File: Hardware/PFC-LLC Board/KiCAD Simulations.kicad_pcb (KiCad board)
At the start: 2 copper layers, 157 x 79.5 mm, 42 parts, among them J1 1792229, J2 Conn_01x02_Female, J3 1792229, Q1 C2M0160120D, U1 UCC28180DR

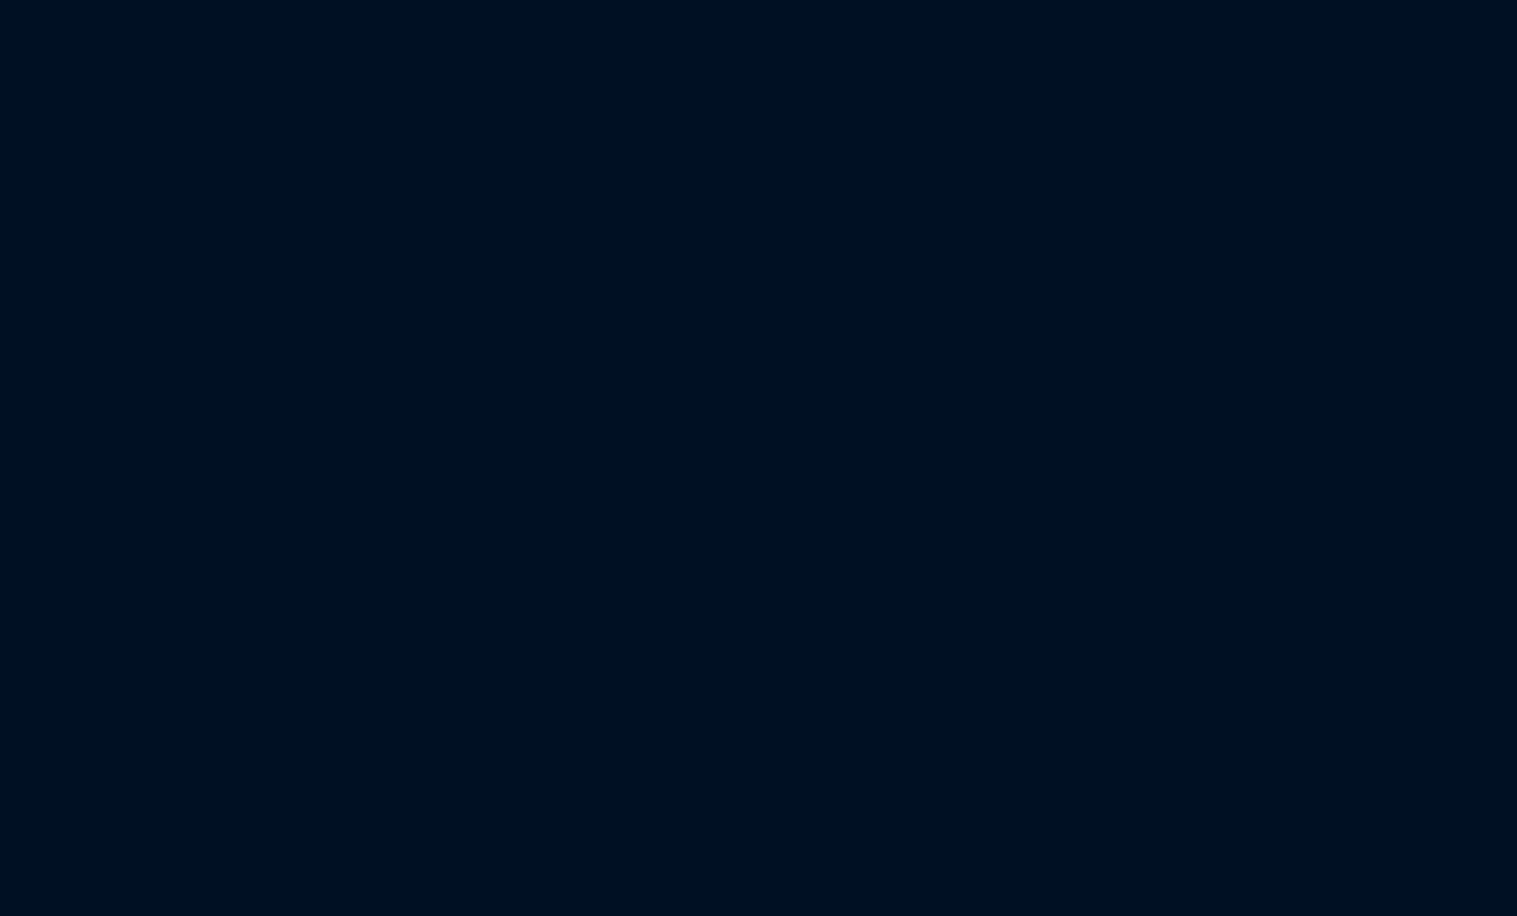
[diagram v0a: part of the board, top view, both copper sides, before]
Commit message: LLC PCB ready w/ PFC board
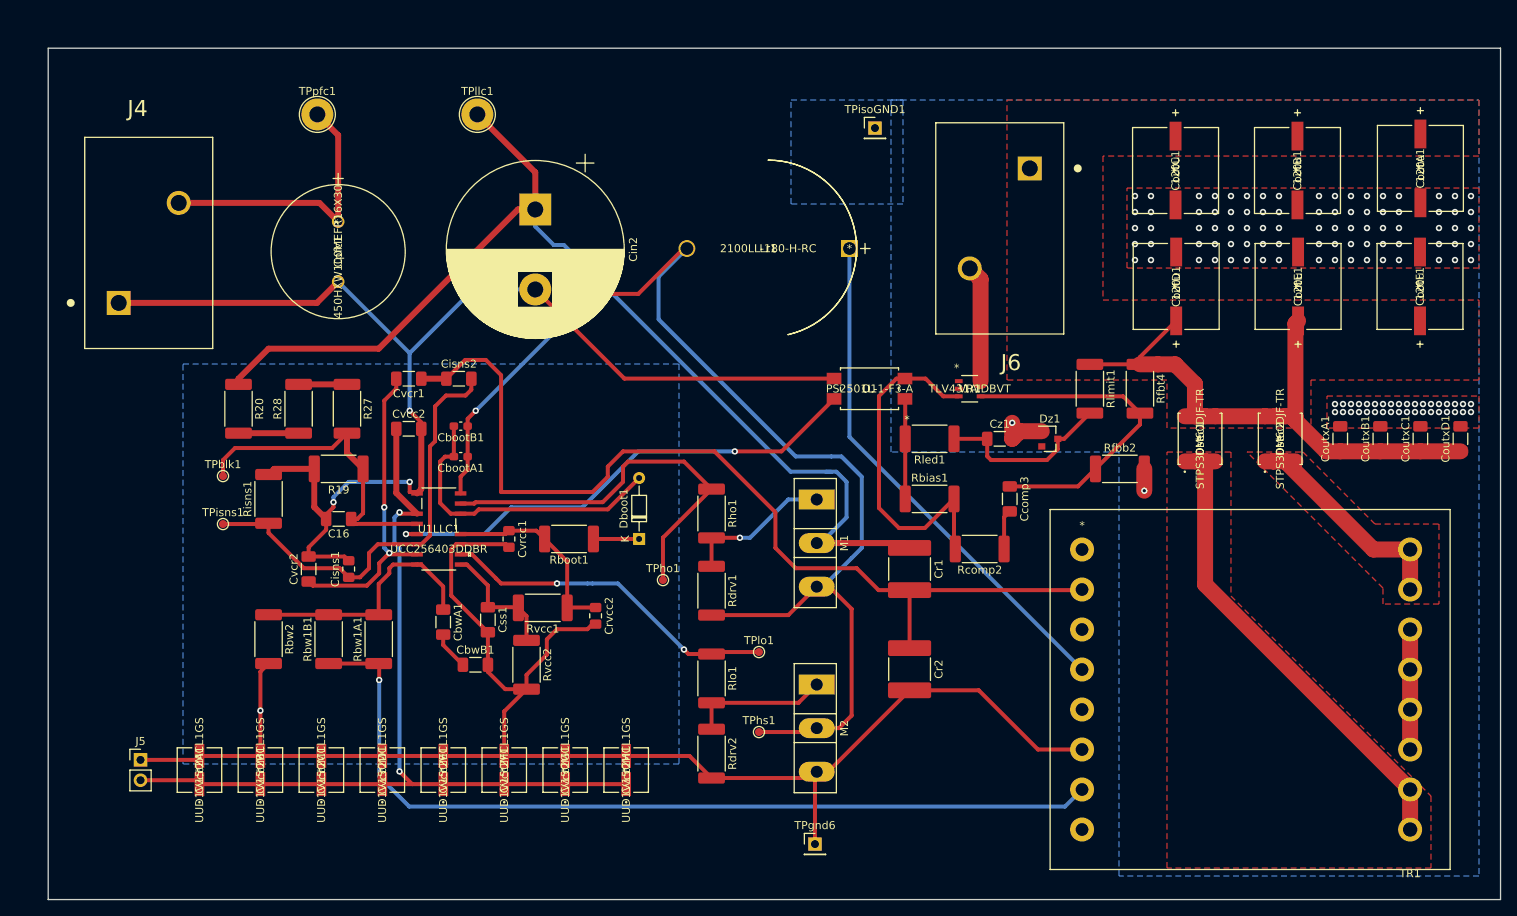
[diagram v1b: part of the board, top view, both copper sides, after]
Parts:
- added C16: 220p, Capacitor_SMD:C_1206_3216Metric_Pad1.33x1.80mm_HandSolder, F.Cu at (131.5, 384.4)
- added CbootA1: 470n, Capacitor_SMD:C_0603_1608Metric_Pad1.08x0.95mm_HandSolder, F.Cu at (146.7, 376.6)
- added CbootB1: 470n, Capacitor_SMD:C_0603_1608Metric_Pad1.08x0.95mm_HandSolder, F.Cu at (146.7, 372.8)
- added CbwA1: 12p, Capacitor_SMD:C_1206_3216Metric_Pad1.33x1.80mm_HandSolder, F.Cu at (144.5, 397.3)
- added CbwB1: 12p, Capacitor_SMD:C_1206_3216Metric_Pad1.33x1.80mm_HandSolder, F.Cu at (148.6, 402.6)
- added Ccomp3: 2.7n, Capacitor_SMD:C_1206_3216Metric_Pad1.33x1.80mm_HandSolder, F.Cu at (215.3, 381.9)
- added Cin2: 47u, Capacitor_THT:CP_Radial_D22.0mm_P10.00mm_SnapIn, F.Cu at (156.0, 345.7)
- added Cisns1: 3.3p, Capacitor_SMD:C_0805_2012Metric_Pad1.18x1.45mm_HandSolder, F.Cu at (132.7, 390.6)
- added Cisns2: 220p, Capacitor_SMD:C_1206_3216Metric_Pad1.33x1.80mm_HandSolder, F.Cu at (146.5, 366.8)
- added CoutA1: 120u, LLC_Cout:35SVPF120M, F.Cu at (266.7, 340.5)
- added CoutB1: 120u, LLC_Cout:35SVPF120M, F.Cu at (251.3, 340.8)
- added CoutC1: 120u, LLC_Cout:35SVPF120M, F.Cu at (236.1, 340.8)
- added CoutD1: 120u, LLC_Cout:35SVPF120M, F.Cu at (236.1, 355.3)
- added CoutE1: 120u, LLC_Cout:35SVPF120M, F.Cu at (251.4, 355.3)
- added CoutF1: 120u, LLC_Cout:35SVPF120M, F.Cu at (266.6, 355.3)
- added CoutxA1: 22u, Capacitor_SMD:C_1206_3216Metric_Pad1.33x1.80mm_HandSolder, F.Cu at (256.7, 374.3)
- added CoutxB1: 22u, Capacitor_SMD:C_1206_3216Metric_Pad1.33x1.80mm_HandSolder, F.Cu at (261.7, 374.3)
- added CoutxC1: 22u, Capacitor_SMD:C_1206_3216Metric_Pad1.33x1.80mm_HandSolder, F.Cu at (266.7, 374.3)
- added CoutxD1: 22u, Capacitor_SMD:C_1206_3216Metric_Pad1.33x1.80mm_HandSolder, F.Cu at (271.7, 374.3)
- added Cpfc1: 450HXW100MEFR16X30, LLC_pfc:450HXW100MEFR16X30, F.Cu at (131.4, 347.2)
- added Cr1: 150n, Capacitor_SMD:C_2220_5650Metric_Pad1.97x5.40mm_HandSolder, F.Cu at (202.8, 390.6)
- added Cr2: 150n, Capacitor_SMD:C_2220_5650Metric_Pad1.97x5.40mm_HandSolder, F.Cu at (202.8, 403.1)
- added Crvcc2: 4.7u, Capacitor_SMD:C_0805_2012Metric_Pad1.18x1.45mm_HandSolder, F.Cu at (163.6, 396.5)
- added Css1: 150n, Capacitor_SMD:C_1206_3216Metric_Pad1.33x1.80mm_HandSolder, F.Cu at (150.1, 397.0)
- added Cvcc2: 2.2u, Capacitor_SMD:C_1206_3216Metric_Pad1.33x1.80mm_HandSolder, F.Cu at (140.2, 373.1)
- added Cvcc2A1: UUD1V150MCL1GS, LLC_Cvcc2:UUD1V150MCL1GS, F.Cu at (114.1, 415.8)
- added Cvcc2B1: UUD1V150MCL1GS, LLC_Cvcc2:UUD1V150MCL1GS, F.Cu at (121.7, 415.8)
- added Cvcc2C1: UUD1V150MCL1GS, LLC_Cvcc2:UUD1V150MCL1GS, F.Cu at (129.3, 415.8)
- added Cvcc2D1: UUD1V150MCL1GS, LLC_Cvcc2:UUD1V150MCL1GS, F.Cu at (136.9, 415.8)
- added Cvcc2E1: UUD1V150MCL1GS, LLC_Cvcc2:UUD1V150MCL1GS, F.Cu at (144.5, 415.8)
- added Cvcc2F1: UUD1V150MCL1GS, LLC_Cvcc2:UUD1V150MCL1GS, F.Cu at (152.2, 415.8)
- added Cvcc2G1: UUD1V150MCL1GS, LLC_Cvcc2:UUD1V150MCL1GS, F.Cu at (159.8, 415.8)
- added Cvcc2H1: UUD1V150MCL1GS, LLC_Cvcc2:UUD1V150MCL1GS, F.Cu at (167.4, 415.8)
- added Cvcr1: 220p, Capacitor_SMD:C_1206_3216Metric_Pad1.33x1.80mm_HandSolder, F.Cu at (140.2, 366.8)
- added Cvcr2: 22n, Capacitor_SMD:C_1206_3216Metric_Pad1.33x1.80mm_HandSolder, F.Cu at (127.7, 390.6)
- added Cvrcc1: 4.7u, Capacitor_SMD:C_0805_2012Metric_Pad1.18x1.45mm_HandSolder, F.Cu at (152.7, 386.9)
- added Cz1: 100n, Capacitor_SMD:C_1206_3216Metric_Pad1.33x1.80mm_HandSolder, F.Cu at (214.1, 374.3)
- added Dboot1: DIODE, Diode_THT:D_DO-34_SOD68_P7.62mm_Horizontal, F.Cu at (169.0, 386.9)
- added Dsec1: STPS30M60DJF-TR, LLC_Dsec:STPS30M60DJF-TR-Modified, F.Cu at (239.1, 374.3)
- added Dsec2: STPS30M60DJF-TR, LLC_Dsec:STPS30M60DJF-TR-Modified, F.Cu at (249.1, 374.3)
- added Dz1: BZX84Cxx, Diode_SMD:D_SOT-23_ANK, F.Cu at (220.4, 374.3)
- added J4: 1792229, Connector2x1:PHOENIX_1792229, F.Cu at (104.0, 357.4)
- added J5: Conn_01x02_Female, Connector_PinHeader_2.54mm:PinHeader_1x02_P2.54mm_Vertical, F.Cu at (106.7, 414.5)
- added J6: 1792229, Connector2x1:PHOENIX_1792229, F.Cu at (217.8, 340.5)
- added Lr1: 2100LL-180-H-RC, LLC_Lr:2100LL-180-H-RC, F.Cu at (195.3, 350.6)
- added M1: IPP060N06N, Package_TO_SOT_THT:TO-247-3_Vertical, F.Cu at (191.2, 381.9)
- added M2: IPP060N06N, Package_TO_SOT_THT:TO-247-3_Vertical, F.Cu at (191.2, 405.1)
- added O1: PS2501L-1-F3-A, LLC_O1:PS2501L-1-F3-A, F.Cu at (197.8, 368.1)
- added R19: 2.7k, Resistor_SMD:R_2512_6332Metric_Pad1.40x3.35mm_HandSolder, F.Cu at (131.5, 378.1)
- added R20: 120k, Resistor_SMD:R_2512_6332Metric_Pad1.40x3.35mm_HandSolder, F.Cu at (118.9, 370.6)
- added R27: 120k, Resistor_SMD:R_2512_6332Metric_Pad1.40x3.35mm_HandSolder, F.Cu at (132.5, 370.6)
- added R28: 100k, Resistor_SMD:R_2512_6332Metric_Pad1.40x3.35mm_HandSolder, F.Cu at (126.5, 370.6)
- added Rbias1: 6.04k, Resistor_SMD:R_2512_6332Metric_Pad1.40x3.35mm_HandSolder, F.Cu at (205.3, 381.9)
- added Rboot1: 2.20, Resistor_SMD:R_2512_6332Metric_Pad1.40x3.35mm_HandSolder, F.Cu at (160.3, 386.9)
- added Rbw1A1: 82k, Resistor_SMD:R_2512_6332Metric_Pad1.40x3.35mm_HandSolder, F.Cu at (136.5, 399.4)
- added Rbw1B1: 82k, Resistor_SMD:R_2512_6332Metric_Pad1.40x3.35mm_HandSolder, F.Cu at (130.2, 399.4)
- added Rbw2: 10k, Resistor_SMD:R_2512_6332Metric_Pad1.40x3.35mm_HandSolder, F.Cu at (122.7, 399.4)
- added Rcomp2: 18.7k, Resistor_SMD:R_2512_6332Metric_Pad1.40x3.35mm_HandSolder, F.Cu at (211.6, 388.1)
- added Rdrv1: 5.11k, Resistor_SMD:R_2512_6332Metric_Pad1.40x3.35mm_HandSolder, F.Cu at (178.1, 393.3)
- added Rdrv2: 5.11k, Resistor_SMD:R_2512_6332Metric_Pad1.40x3.35mm_HandSolder, F.Cu at (178.1, 413.7)
- added Rfbb2: 8.06k, Resistor_SMD:R_2512_6332Metric_Pad1.40x3.35mm_HandSolder, F.Cu at (229.1, 378.1)
- added Rfbt4: 110k, Resistor_SMD:R_2512_6332Metric_Pad1.40x3.35mm_HandSolder, F.Cu at (231.6, 368.1)
- added Rho1: 1, Resistor_SMD:R_2512_6332Metric_Pad1.40x3.35mm_HandSolder, F.Cu at (178.1, 383.7)
- added Risns1: 390, Resistor_SMD:R_2512_6332Metric_Pad1.40x3.35mm_HandSolder, F.Cu at (122.7, 381.9)
- added Rled1: 36.5k, Resistor_SMD:R_2512_6332Metric_Pad1.40x3.35mm_HandSolder, F.Cu at (205.3, 374.3)
- added Rlimit1: 18.2k, Resistor_SMD:R_2512_6332Metric_Pad1.40x3.35mm_HandSolder, F.Cu at (225.4, 368.1)
- added Rlo1: 1, Resistor_SMD:R_2512_6332Metric_Pad1.40x3.35mm_HandSolder, F.Cu at (178.1, 404.3)
- added Rvcc1: 220k, Resistor_SMD:R_2512_6332Metric_Pad1.40x3.35mm_HandSolder, F.Cu at (157.0, 395.5)
- added Rvcc2: 1.2M, Resistor_SMD:R_2512_6332Metric_Pad1.40x3.35mm_HandSolder, F.Cu at (154.9, 402.6)
- added TPblk1: TestPoint, TestPoint:TestPoint_Pad_D1.0mm, F.Cu at (117.0, 379.0)
- added TPgnd6: TestPoint, Connector_PinHeader_2.54mm:PinHeader_1x01_P2.54mm_Vertical, F.Cu at (191.0, 425.0)
- added TPho1: TestPoint, TestPoint:TestPoint_Pad_D1.0mm, F.Cu at (172.0, 392.0)
- added TPhs1: TestPoint, TestPoint:TestPoint_Pad_D1.0mm, F.Cu at (184.0, 411.0)
- added TPisns1: TestPoint, TestPoint:TestPoint_Pad_D1.0mm, F.Cu at (117.0, 385.0)
- added TPisoGND1: TestPoint, Connector_PinHeader_2.54mm:PinHeader_1x01_P2.54mm_Vertical, F.Cu at (198.5, 335.5)
- added TPllc1: TestPoint, TestPoint:TestPoint_THTPad_D4.0mm_Drill2.0mm, F.Cu at (148.8, 333.8)
- added TPlo1: TestPoint, TestPoint:TestPoint_Pad_D1.0mm, F.Cu at (184.0, 401.0)
- added TPpfc1: TestPoint, TestPoint:TestPoint_THTPad_D4.0mm_Drill2.0mm, F.Cu at (128.8, 333.8)
- added TR1: TRANSF6-WE, LLC_Transformer:Transformer, F.Cu at (245.4, 428.2)
- added U1LLC1: UCC256403DDBR, LLC_U1:UCC256403DDBR, F.Cu at (144.0, 385.6)
- added VR1: TLV431AIDBVT, LLC_VR1:TLV431AIDBVT, F.Cu at (210.3, 368.1)
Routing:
- net GND: track 371.7 -> 735.2 mm, vias 3 -> 7
- net /LLC/HS: track 0.00 -> 152.2 mm, vias 0 -> 2
- net Net-(Cin2-Pad1): track 0.00 -> 137.7 mm
- net Net-(Cisns2-Pad1): track 0.00 -> 118.9 mm
- net Net-(Rbw1A1-Pad1): track 0.00 -> 110.7 mm, vias 0 -> 1
- net Net-(Cvcc2-Pad1): track 0.00 -> 110.0 mm, vias 0 -> 2
- net Net-(CoutA1-Pad1): track 0.00 -> 74.1 mm
- net Net-(Lr1-Pad1): track 0.00 -> 64.7 mm
- net Net-(O1-Pad4): track 0.00 -> 61.9 mm, vias 0 -> 2
- net Net-(Dsec1-Pad1): track 0.00 -> 60.4 mm
- net Net-(Cisns1-Pad1): track 0.00 -> 56.2 mm
- net /LLC/HO: track 0.00 -> 50.0 mm
- net Net-(O1-Pad2): track 0.00 -> 44.0 mm
- net /LLC/LO: track 0.00 -> 42.6 mm, vias 0 -> 2
- net Net-(Ccomp3-Pad1): track 0.00 -> 41.7 mm
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- added copper zone on B.Cu, net GND
- added copper zone on B.Cu, net GND1
- added copper zone on F.Cu, net GND1
- added copper zone on F.Cu, net Net-(CoutA1-Pad1)
- added copper zone on F.Cu, net Net-(Dsec1-Pad1)
- added copper zone on F.Cu, net Net-(Dsec2-Pad1)
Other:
- board size 157 x 79.5 mm -> 186 x 412.4 mm

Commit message: LLC gerber files generated
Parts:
- removed Ccomp1: 22u, Capacitor_SMD:C_1206_3216Metric_Pad1.33x1.80mm_HandSolder
- removed Ccomp2: 560n, Capacitor_SMD:C_1206_3216Metric_Pad1.33x1.80mm_HandSolder
- removed Cicomp1: 3.3n, Capacitor_SMD:C_1206_3216Metric_Pad1.33x1.80mm_HandSolder
- removed Cin1, Coutx1, Coutx2: 100n, Capacitor_THT:CP_Axial_L34.5mm_D20.0mm_P41.00mm_Horizontal
- removed Cisense1: 1n, Capacitor_SMD:C_1206_3216Metric_Pad1.33x1.80mm_HandSolder
- removed Cvcc1: 1u, Capacitor_SMD:C_1206_3216Metric_Pad1.33x1.80mm_HandSolder
- removed Cvccx1: 100n, Capacitor_SMD:C_1206_3216Metric_Pad1.33x1.80mm_HandSolder
- removed Cvsense1: 4.7n, Capacitor_SMD:C_1206_3216Metric_Pad1.33x1.80mm_HandSolder
- removed Dboost1: UF5406, Diode_THT:D_DO-201AD_P15.24mm_Horizontal
- removed Disense1: 1N4148, Diode_THT:D_DO-35_SOD27_P7.62mm_Horizontal
- removed Dstart1: C3D10060A, Package_TO_SOT_THT:TO-220-2_Vertical
- removed Dturnoff1: B240, Diode_SMD:D_SMB
- removed J1, J3: 1792229, Connector2x1:PHOENIX_1792229
- removed J2: Conn_01x02_Female, Connector_PinHeader_2.54mm:PinHeader_1x02_P2.54mm_Vertical
- removed L1: 197.691u, PFC_L1:IND_FIT106-2
- removed Q1: C2M0160120D, Package_TO_SOT_THT:TO-247-3_Vertical
- removed Rcomp1: 15.4k, Resistor_SMD:R_2512_6332Metric_Pad1.40x3.35mm_HandSolder
- removed Rfbb1: 12.1k, Resistor_SMD:R_2512_6332Metric_Pad1.40x3.35mm_HandSolder
- removed Rfbt1, Rfbt3: 300k, Resistor_SMD:R_2512_6332Metric_Pad1.40x3.35mm_HandSolder
- removed Rfbt2: 402k, Resistor_SMD:R_2512_6332Metric_Pad1.40x3.35mm_HandSolder
- removed Rfreq1: 17.4k, Resistor_SMD:R_2512_6332Metric_Pad1.40x3.35mm_HandSolder
- removed Rgate1: 1.00, Resistor_SMD:R_2512_6332Metric_Pad1.40x3.35mm_HandSolder
- removed Rgate2: 10k, Resistor_SMD:R_2512_6332Metric_Pad1.40x3.35mm_HandSolder
- removed Rgate3: 3.92, Resistor_SMD:R_2512_6332Metric_Pad1.40x3.35mm_HandSolder
- removed Risense1: 221, Resistor_SMD:R_2512_6332Metric_Pad1.40x3.35mm_HandSolder
- removed Rntc1: 1, Resistor_THT:R_Box_L13.0mm_W4.0mm_P9.00mm
- removed Rsense1: 15m, Resistor_SMD:R_2512_6332Metric_Pad1.40x3.35mm_HandSolder
- removed TPDstart1: TestPoint Dstart, TestPoint:TestPoint_Pad_D1.0mm
- removed TPDstart2: TestPoint Dstart2, TestPoint:TestPoint_Pad_D1.0mm
- removed TPQ1: TestPoint Q1, TestPoint:TestPoint_Pad_D1.0mm
- removed TPgate1: TestPoint Gate Pin, TestPoint:TestPoint_Pad_D1.0mm
- removed TPgnd1, TPgnd2: TestPoint GND, TestPoint:TestPoint_Pad_D1.0mm
- removed TPgnd5: TestPoint GND Q1, TestPoint:TestPoint_Pad_D1.0mm
- removed TPisense1, TPvsense1: TestPoint, TestPoint:TestPoint_Pad_D1.0mm
- removed U1: UCC28180DR, PFC_IC:UCC28180DR
- removed Uac1: GBJ2510-F, PFC_Dac:GBJ2510-F
- moved C16 295.6 mm to (88.5, 91.9)
- moved CbootA1 295.6 mm to (103.7, 84.1)
- moved CbootB1 295.6 mm to (103.7, 80.3)
- moved CbwA1 295.6 mm to (101.5, 104.8)
- moved CbwB1 295.6 mm to (105.6, 110.1)
- moved Ccomp3 295.6 mm to (172.3, 89.4)
- moved Cin2 295.6 mm to (113.0, 53.2)
- moved Cisns1 295.6 mm to (89.7, 98.1)
- moved Cisns2 295.6 mm to (103.5, 74.3)
- moved CoutA1 295.6 mm to (223.7, 48.0)
- moved CoutB1 295.6 mm to (208.3, 48.3)
- moved CoutC1 295.6 mm to (193.1, 48.3)
- moved CoutD1 295.6 mm to (193.1, 62.8)
- moved CoutE1 295.6 mm to (208.4, 62.8)
- moved CoutF1 295.6 mm to (223.6, 62.8)
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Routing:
- net GND: track 735.2 -> 363.5 mm, vias 7 -> 4
- net Net-(Cin1-Pad2): track 142.4 -> 0.00 mm, vias 1 -> 0
- net Net-(Coutx1-Pad1): track 131.4 -> 0.00 mm
- net Net-(Cin1-Pad1): track 83.2 -> 0.00 mm
- net Net-(Cvsense1-Pad1): track 80.8 -> 0.00 mm
- net Net-(Dboost1-Pad2): track 77.8 -> 0.00 mm
- net Net-(Rfreq1-Pad1): track 65.9 -> 0.00 mm
- net Net-(Cisense1-Pad1): track 52.4 -> 0.00 mm
- net Net-(Cicomp1-Pad1): track 48.9 -> 0.00 mm
- net Net-(Ccomp1-Pad1): track 36.4 -> 0.00 mm, vias 2 -> 0
- net Net-(Cvcc1-Pad1): track 36.0 -> 0.00 mm, vias 2 -> 0
- net Net-(Dturnoff1-Pad2): track 33.2 -> 0.00 mm
- net Net-(Rgate1-Pad1): track 26.2 -> 0.00 mm
- net Net-(J1-Pad2): track 18.8 -> 0.00 mm
- net Net-(J1-Pad1): track 15.2 -> 0.00 mm
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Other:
- board size 186 x 412.4 mm -> 181.5 x 106.4 mm

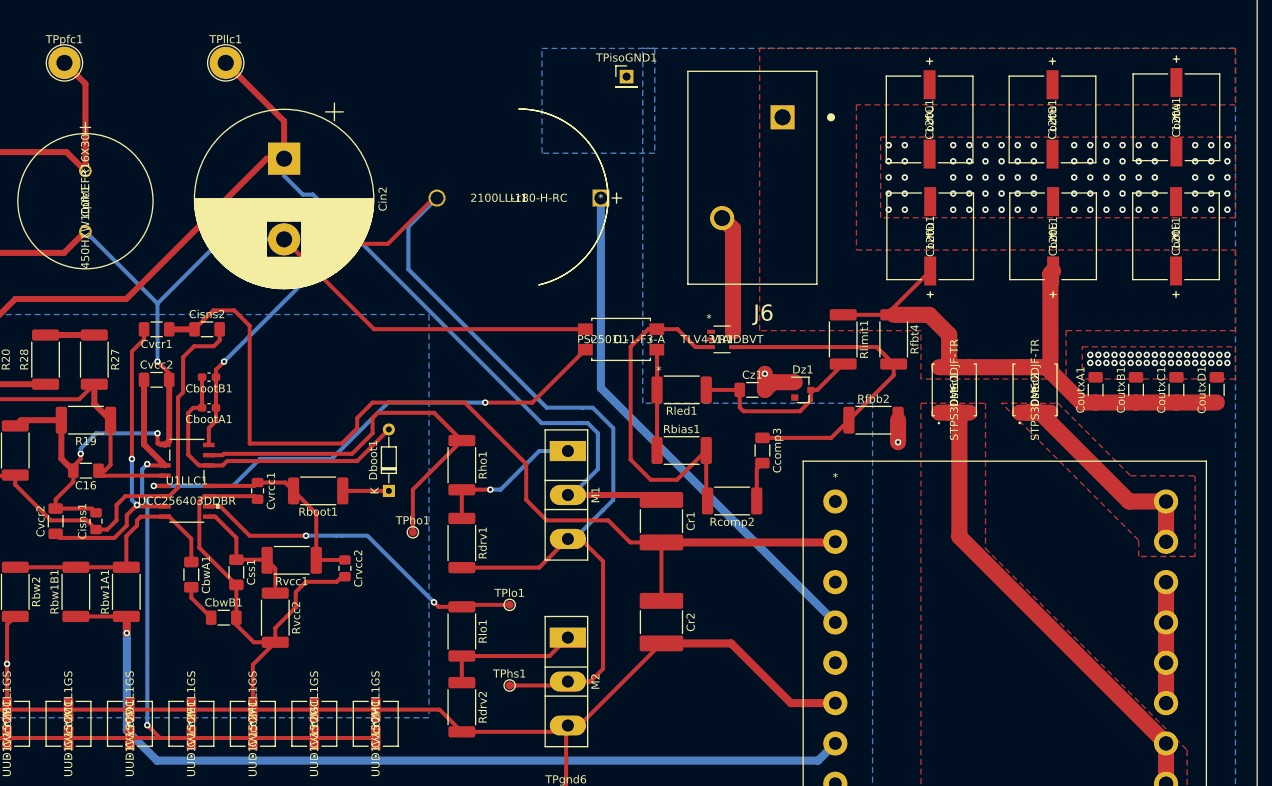
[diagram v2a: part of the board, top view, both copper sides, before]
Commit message: LLC gerber files regenerated
2512 footprints updated to 1206 for Rlimit, Rcomp, drv1, drv2
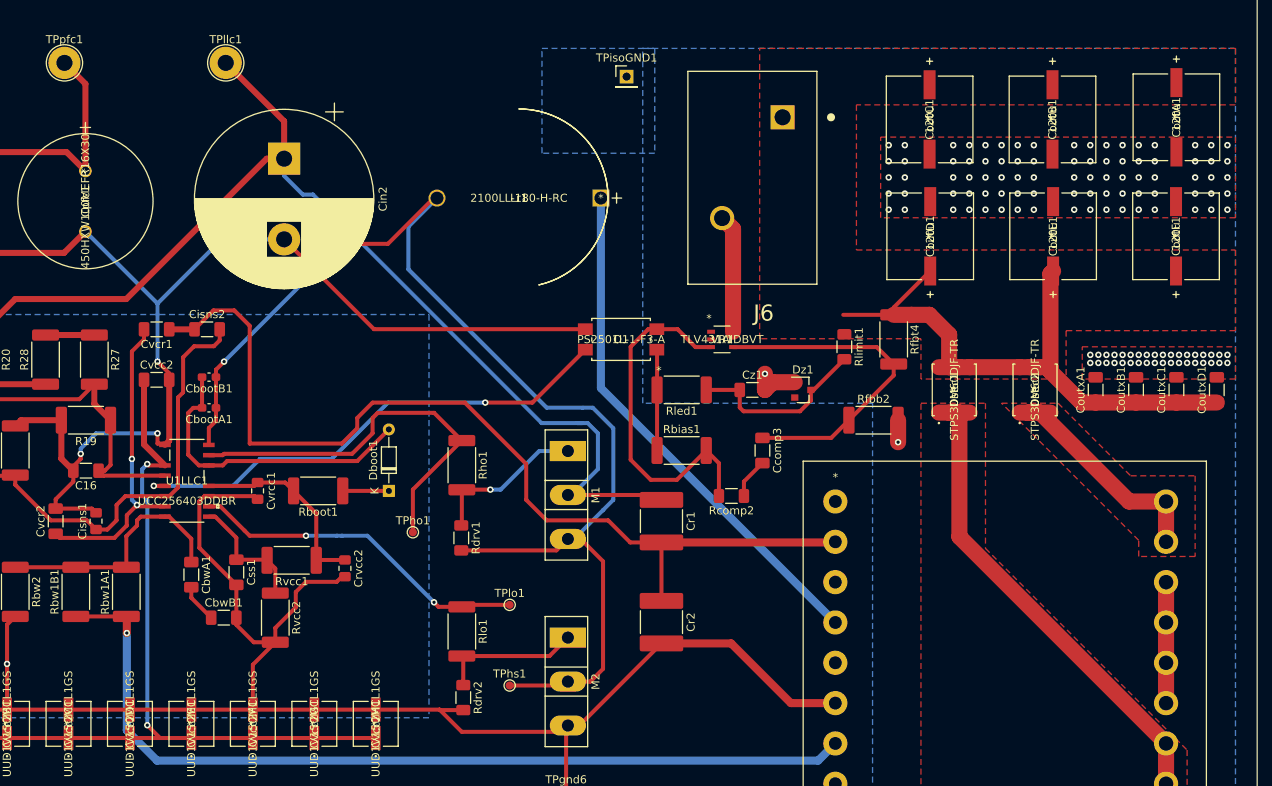
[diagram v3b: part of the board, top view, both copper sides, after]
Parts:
- Rcomp2, Rdrv1, Rdrv2, Rlimit1: footprint Resistor_SMD:R_2512_6332Metric_Pad1.40x3.35mm_HandSolder -> Resistor_SMD:R_1206_3216Metric_Pad1.30x1.75mm_HandSolder
- moved Rdrv2 1.21 mm to (135.2, 120.0)
- moved Rlimit1 0.92 mm to (182.5, 76.5)
- moved Rdrv1 0.64 mm to (135.0, 100.2)
- moved Rcomp2 0.63 mm to (168.5, 95.0)
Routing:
- net GND: track 363.5 -> 366.5 mm
- net Net-(M1-Pad1): track 18.7 -> 19.6 mm
- net /LLC/HS: track 152.2 -> 151.4 mm
- net Net-(M2-Pad1): track 17.4 -> 18.0 mm
